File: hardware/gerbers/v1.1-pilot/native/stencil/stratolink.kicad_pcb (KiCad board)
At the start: 2 copper layers, 23.4 x 57.3 mm, 68 parts, among them J1 Solar panel direct solder, J2 Solar panel direct solder, J20 Conn_ARM_SWD_TagConnect_TC203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, J3 Programming_1x07_P1.00mm_D0.5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, J4 Programming_1x07_P1.00mm_D0.5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, U1 BQ25570RGRR, U2 RAK3172-8-SM-NI, U3 MAX-M10S-00B, U4 MS561101BA03-50, U5 TMP117AIYBGR, U6 AS7331-AQFM, U7 LIS2DH12TR, U8 TLV8801DBVT

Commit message: Regenerate pilot exports and bind final review evidence
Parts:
- moved AE2 16.5 mm to (55.3, 47.9), turned to 180 degrees
- moved D3 8.00 mm to (58.0, 45.0), turned to -90 degrees
- moved C5 1.80 mm to (66.7, 64.7)
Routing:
- net GND: track 273.3 -> 261.6 mm, vias 85 -> 86
- net Net-(AE2-A): track 17.8 -> 6.57 mm
- net /SC_MID: track 22.1 -> 15.5 mm
- net /VBAT: track 27.0 -> 28.9 mm
- net /SC_BAL_OUT: track 15.4 -> 16.3 mm
- net +3.3V: track 152.7 -> 151.9 mm
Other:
- board text added: "GNSS: 48 mm straight wire LEFT from feed; tune assembled payload"

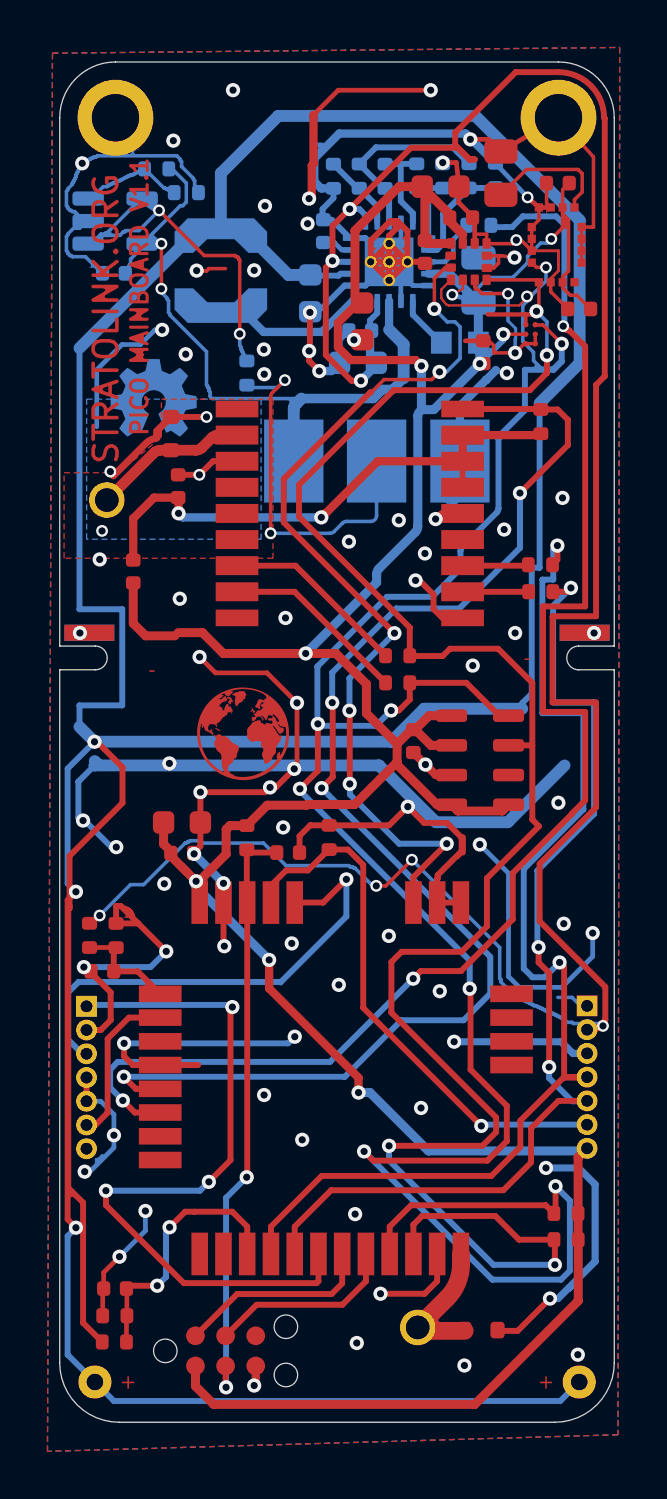
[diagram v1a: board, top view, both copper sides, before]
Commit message: Regenerate pilot manufacturing files for upward GNSS layout
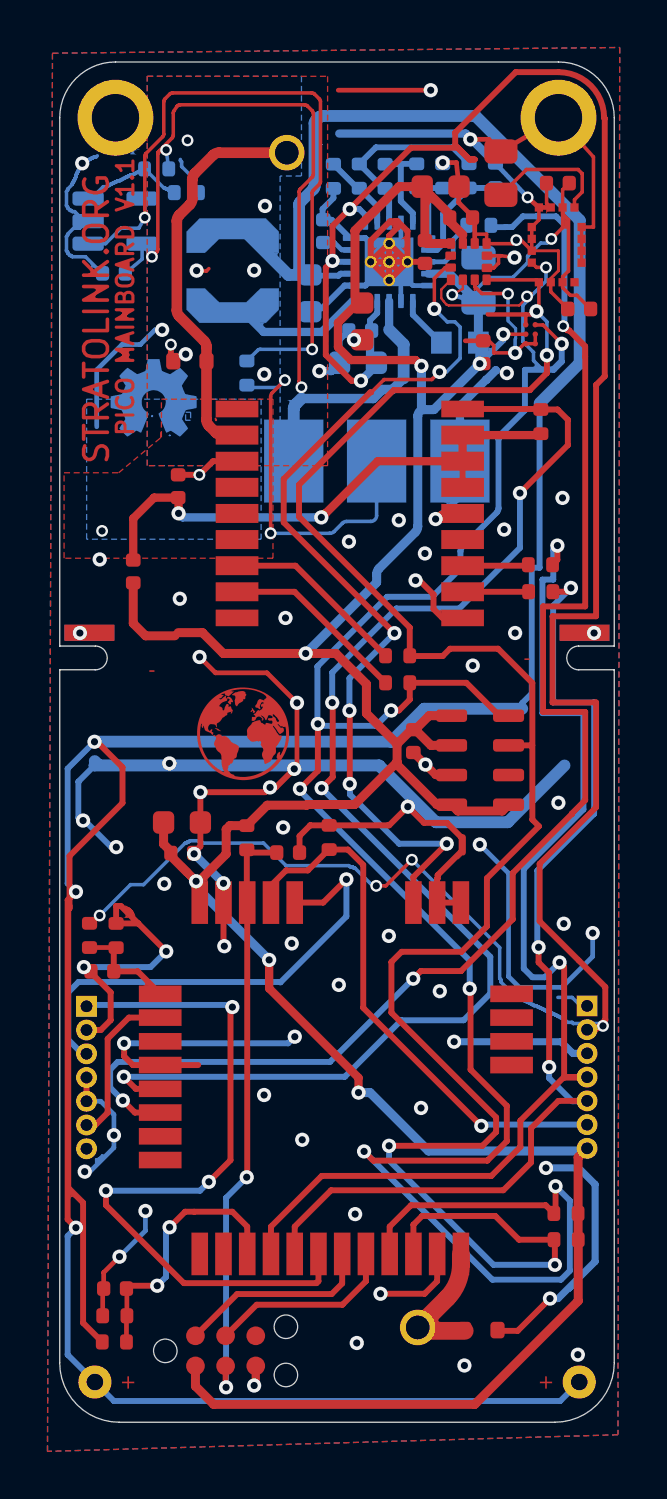
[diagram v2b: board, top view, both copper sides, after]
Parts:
- moved AE2 16.5 mm to (62.9, 33.2), turned to 90 degrees
- moved D3 3.15 mm to (58.8, 42.0), turned to 0 degrees
- moved L1 0.50 mm to (60.6, 38.2)
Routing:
- net +SOLAR: track 172.5 -> 143.4 mm
- net GND: track 261.6 -> 245.3 mm, vias 86 -> 79
- net /SC_BAL_OUT: track 16.3 -> 29.5 mm
- net /VBAT: track 28.9 -> 39.3 mm, vias 2 -> 3
- net Net-(AE2-A): track 6.57 -> 16.9 mm
- net Net-(U1-LBOOST): track 6.97 -> 6.47 mm
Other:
- board text added: "GNSS: 48 mm straight wire UP from top feed; tune assembled payload"
- board text removed: "GNSS: 48 mm straight wire LEFT from feed; tune assembled payload"

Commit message: Rebuild pilot manufacturing and KiCad downloads from engineer review
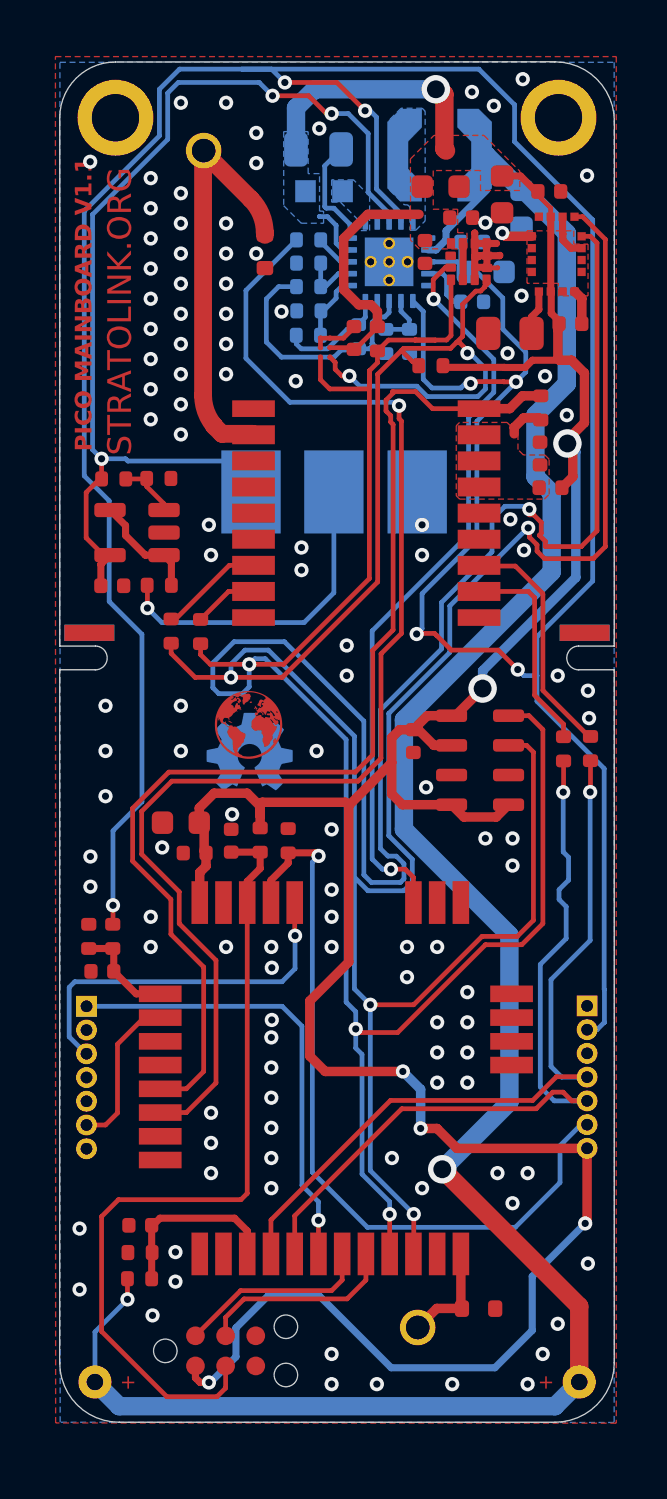
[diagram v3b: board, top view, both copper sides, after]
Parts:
- C22, R24, R25, R26, U8: moved to F.Cu
- moved R12 37.7 mm to (66.7, 41.1), turned to -90 degrees
- moved R11 37.3 mm to (69.0, 42.2)
- moved FB1 17.9 mm to (74.0, 47.3), turned to 0 degrees
- moved C10 15.3 mm to (73.5, 45.9)
- moved R24 13.2 mm to (55.6, 47.0), turned to 0 degrees
- moved C22 13.2 mm to (55.5, 51.5), turned to 0 degrees
- moved U8 13.2 mm to (56.6, 49.2), turned to 180 degrees
- moved R25 12.1 mm to (57.5, 46.9)
- moved L1 9.98 mm to (69.3, 33.3), turned to 0 degrees
- moved R26 9.67 mm to (57.5, 51.4), turned to 180 degrees
- moved R14 9.60 mm to (58.0, 53.4), turned to -90 degrees
- moved C2 9.58 mm to (72.8, 35.6)
- moved C6 8.70 mm to (64.2, 33.1), turned to 180 degrees
- moved R7 8.69 mm to (63.8, 37.9), turned to 180 degrees
- moved U5 8.67 mm to (64.5, 41.4), turned to 180 degrees
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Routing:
- net GND: track 245.3 -> 17.4 mm, vias 79 -> 117
- net +SOLAR: track 143.4 -> 92.0 mm, vias 3 -> 2
- net VSTOR: track 104.4 -> 143.4 mm
- net SDA: track 87.3 -> 125.1 mm, vias 4 -> 6
- net SCL: track 99.0 -> 134.4 mm, vias 9 -> 4
- net /SC_BAL_OUT: track 29.5 -> 4.70 mm, vias 2 -> 0
- net Net-(U3-VCC): track 23.2 -> 1.59 mm, vias 2 -> 0
- net TX: track 47.5 -> 32.5 mm, vias 2 -> 1
- net PA1: track 30.6 -> 19.3 mm, vias 3 -> 1
- net +3.3V: track 151.9 -> 141.1 mm, vias 9 -> 7
- net RX: track 43.1 -> 33.0 mm, vias 3 -> 1
- net RST: track 25.2 -> 34.6 mm, vias 2 -> 0
- net BOOT0: track 23.0 -> 32.4 mm
- net RSTN: track 56.2 -> 48.2 mm, vias 4 -> 0
- net Net-(U3-RXD): track 2.79 -> 10.1 mm
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- added copper zone on B.Cu, net +3.3V
- added copper zone on F.Cu, net +3.3V
- added copper zone on B.Cu, net Net-(U1-LBOOST)
- added copper zone on B.Cu, net Net-(U1-LBUCK)
- added copper zone on F.Cu, net Net-(U3-VCC)
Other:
- outline, holes or cut-outs redrawn
- board text removed: "GNSS: 48 mm straight wire UP from top feed; tune assembled payload"
